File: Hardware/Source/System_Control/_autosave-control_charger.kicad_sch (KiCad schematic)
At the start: 20 parts, among them Q21 IRF540NPbF, Q22 IRF540NPbF, Q23 MMBT2222A, Q24 MMBT2222A, U24 PC817X2NIPW, U25 PC817X2NIPW

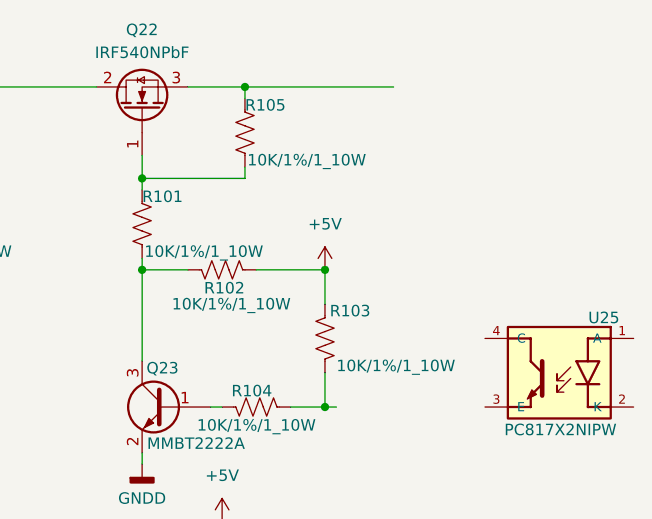
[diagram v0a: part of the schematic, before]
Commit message: update sche control system
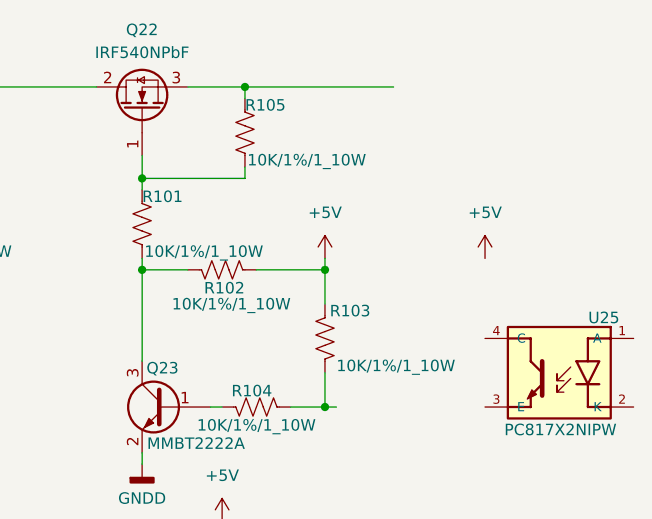
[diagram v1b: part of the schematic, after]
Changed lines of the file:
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@@
+	(wire
+		(pts
+			(xy 181.61 77.47) (xy 181.61 78.74)
+		)
+		(stroke
+			(width 0)
+			(type default)
+		)
+	)
 	(wire
 		(pts
@@
 	(symbol
 		(lib_id "power:+5V")
-		(at 181.61 78.74 0)
+		(at 181.61 77.47 0)
 		(unit 1)
 		(exclude_from_sim no)
@@
 		(fields_autoplaced yes)
 		(property "Reference" "#PWR0107"
-			(at 181.61 82.55 0)
+			(at 181.61 81.28 0)
 			(effects
 				(font
@@
 		)
 		(property "Value" "+5V"
-			(at 181.61 73.66 0)
+			(at 181.61 72.39 0)
 			(effects
 				(font
@@
 		)
 		(property "Footprint" ""
-			(at 181.61 78.74 0)
+			(at 181.61 77.47 0)
 			(effects
 				(font
@@
 		)
 		(property "Datasheet" ""
-			(at 181.61 78.74 0)
+			(at 181.61 77.47 0)
 			(effects
 				(font
@@
 		)
 		(property "Description" "Power symbol creates a global label with name \"+5V\""
-			(at 181.61 78.74 0)
+			(at 181.61 77.47 0)
 			(effects
 				(font
@@
 					(unit 1)
 				)
+			)
+		)
+	)
+	(symbol
+		(lib_id "power:+5V")
+		(at 199.39 77.47 0)
+		(unit 1)
+		(exclude_from_sim no)
+		(in_bom yes)
+		(on_board yes)
+		(dnp no)
+		(fields_autoplaced yes)
+		(property "Reference" "#PWR0113"
+			(at 199.39 81.28 0)
+			(effects
+				(font
+					(size 1.27 1.27)
+				)
+				(hide yes)
+			)
+		)
+		(property "Value" "+5V"
+			(at 199.39 72.39 0)
+			(effects
+				(font
+					(size 1.27 1.27)
+				)
+			)
+		)
+		(property "Footprint" ""
+			(at 199.39 77.47 0)
+			(effects
+				(font
+					(size 1.27 1.27)
+				)
+				(hide yes)
+			)
+		)
+		(property "Datasheet" ""
+			(at 199.39 77.47 0)
+			(effects
+				(font
+					(size 1.27 1.27)
+				)
+				(hide yes)
+			)
+		)
+		(property "Description" "Power symbol creates a global label with name \"+5V\""
+			(at 199.39 77.47 0)
+			(effects
+				(font
+					(size 1.27 1.27)
+				)
+				(hide yes)
+			)
+		)
+		(pin "1"
+		)
+		(instances
+			(project "System_Control"
+				(path "/85c53e8c-0403-413d-b6c5-0718d4365b1f/dcdba039-ea40-479a-8e78-13cd4769be17"
+					(reference "#PWR0113")
+					(unit 1)
+				)
